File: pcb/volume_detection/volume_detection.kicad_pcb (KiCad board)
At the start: 2 copper layers, 80 x 36 mm, 30 parts, among them J1 Avr ISP, J2 Sens 1, J3 Sens 2, J4 12v DC, U1 MC34063AD, U2 ATmega328P-PU

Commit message: update pcb
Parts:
- C1, C3: value 100uf -> 100nf
- J4: value 12v DC -> +12v
- L1: footprint Inductor_THT:L_Axial_L5.3mm_D2.2mm_P10.16mm_Horizontal_Vishay_IM-1 -> Inductor_THT:L_Axial_L7.0mm_D3.3mm_P5.08mm_Vertical_Fastron_MICC
- L2: footprint Inductor_THT:L_Axial_L5.3mm_D2.2mm_P10.16mm_Horizontal_Vishay_IM-1 -> Inductor_THT:L_Axial_L6.6mm_D2.7mm_P10.16mm_Horizontal_Vishay_IM-2
- R7, R9: value 250 -> 240
- moved L2 1.77 mm to (99.5, 131.3)
- moved C2 1.70 mm to (100.5, 144.0)
- moved L1 1.06 mm to (103.5, 140.8)
- moved R2 0.35 mm to (108.6, 127.5)
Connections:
- R2 pad 2: GND -> Net-(R1-Pad1)
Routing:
- net Net-(R1-Pad1): track 2.54 -> 13.6 mm
- net Net-(Co1-Pad1): track 9.74 -> 17.4 mm
- net Net-(D1-Pad1): track 14.3 -> 15.9 mm, vias 0 -> 1
- net +5V: track 124.1 -> 122.6 mm
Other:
- board text added: "Volume detection V1.1"
- board text removed: "Volume detection V1.0"

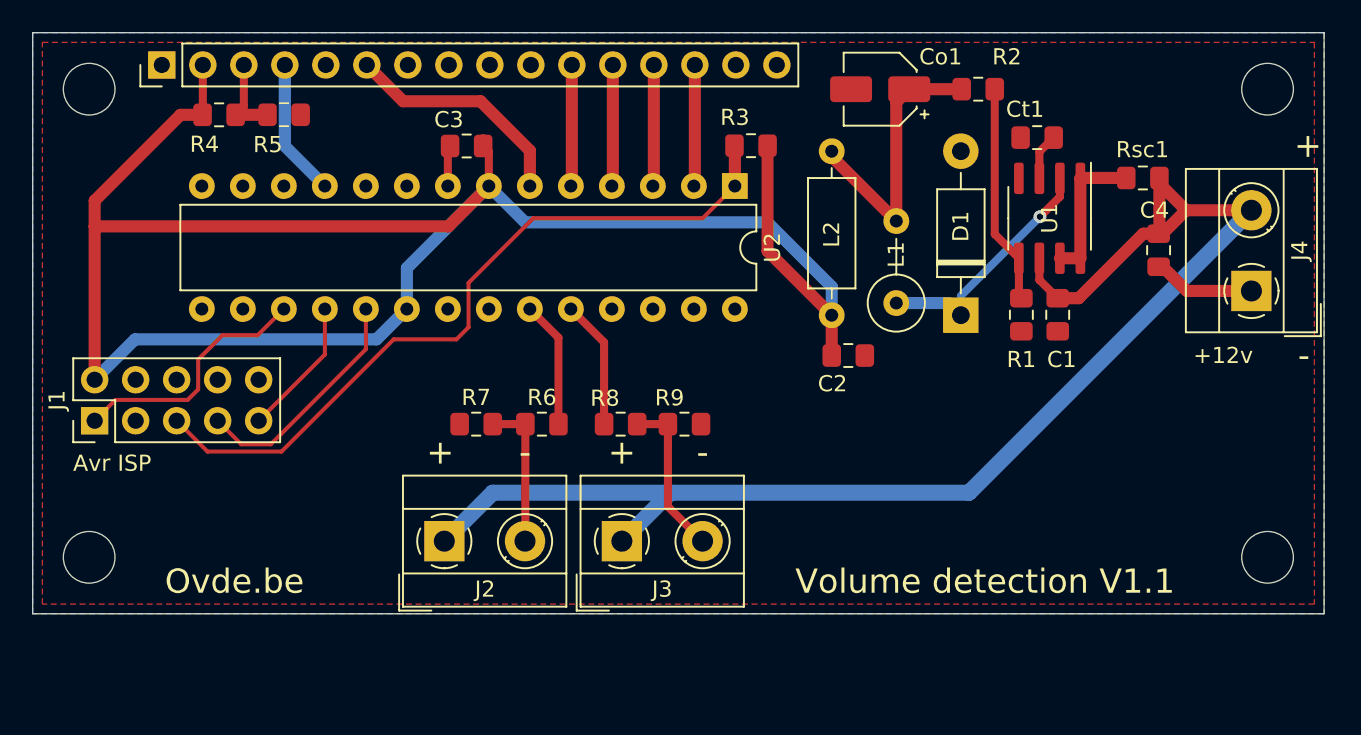
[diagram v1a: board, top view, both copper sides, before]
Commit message: update pcb + adc driver
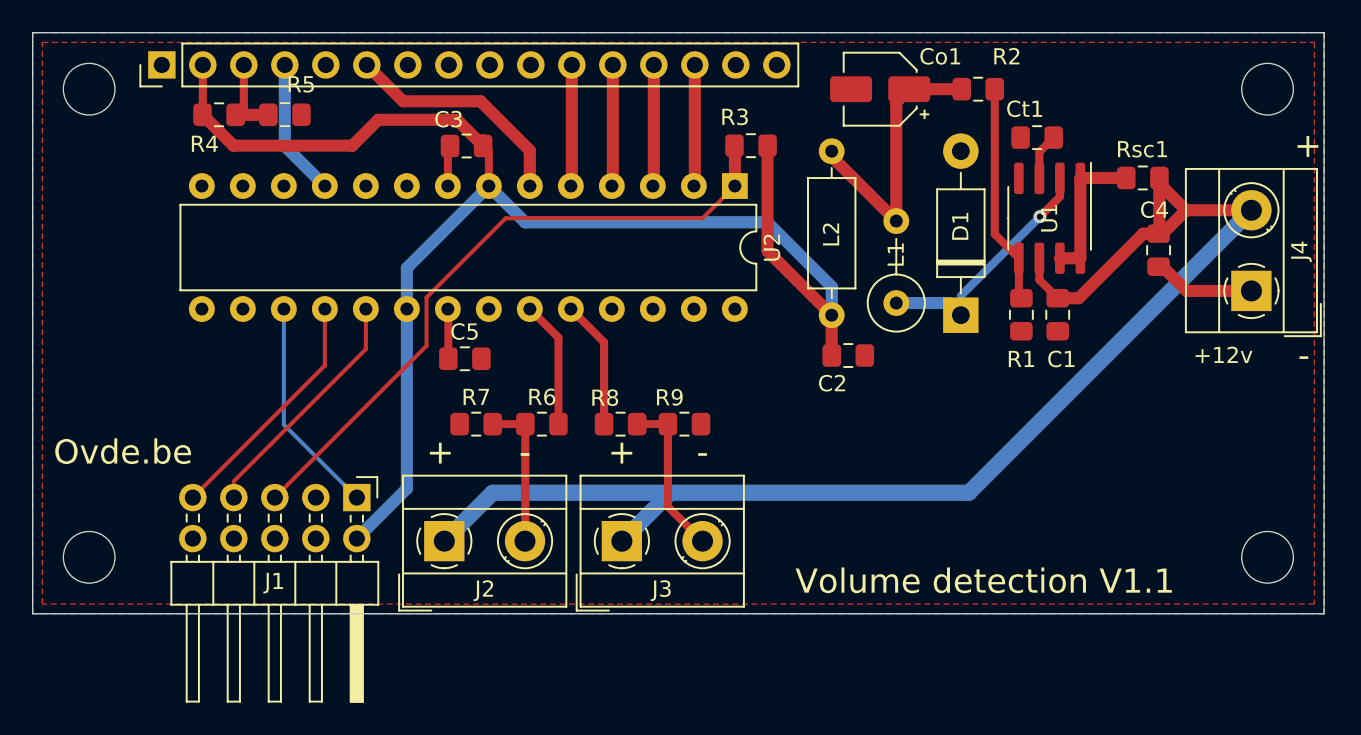
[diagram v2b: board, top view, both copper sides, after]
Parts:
- added C5: 100nf, Capacitor_SMD:C_0805_2012Metric_Pad1.15x1.40mm_HandSolder, F.Cu at (76.8, 144.2)
- J1: footprint Connector_PinHeader_2.54mm:PinHeader_2x05_P2.54mm_Vertical -> Connector_PinHeader_2.54mm:PinHeader_2x05_P2.54mm_Horizontal
- moved J1 16.9 mm to (70.1, 152.8), turned to 270 degrees
- moved R5 0.05 mm to (65.6, 129.1), turned to 180 degrees
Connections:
- LCd1 pad 5: Net-(LCd1-Pad5) -> GND
- R5 pad 1: Net-(LCd1-Pad3) -> GND
- R5 pad 2: GND -> Net-(LCd1-Pad3)
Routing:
- net +5V: track 122.6 -> 91.1 mm
- net /MISO: track 8.62 -> 15.1 mm
- net /RST: track 46.3 -> 40.8 mm
- net Net-(C5-Pad1): track 0.00 -> 3.09 mm
- net /MOSI: track 15.7 -> 13.6 mm
